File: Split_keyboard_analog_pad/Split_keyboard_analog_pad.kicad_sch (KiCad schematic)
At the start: 138 parts, among them J1 Conn_01x05_Pin, J2 Conn_01x05_Pin, J3 Conn_01x08_Pin, J4 Conn_01x08_Pin, J5 Conn_01x02, J6 Conn_01x02, U1 nice_nano, U2 nice_nano

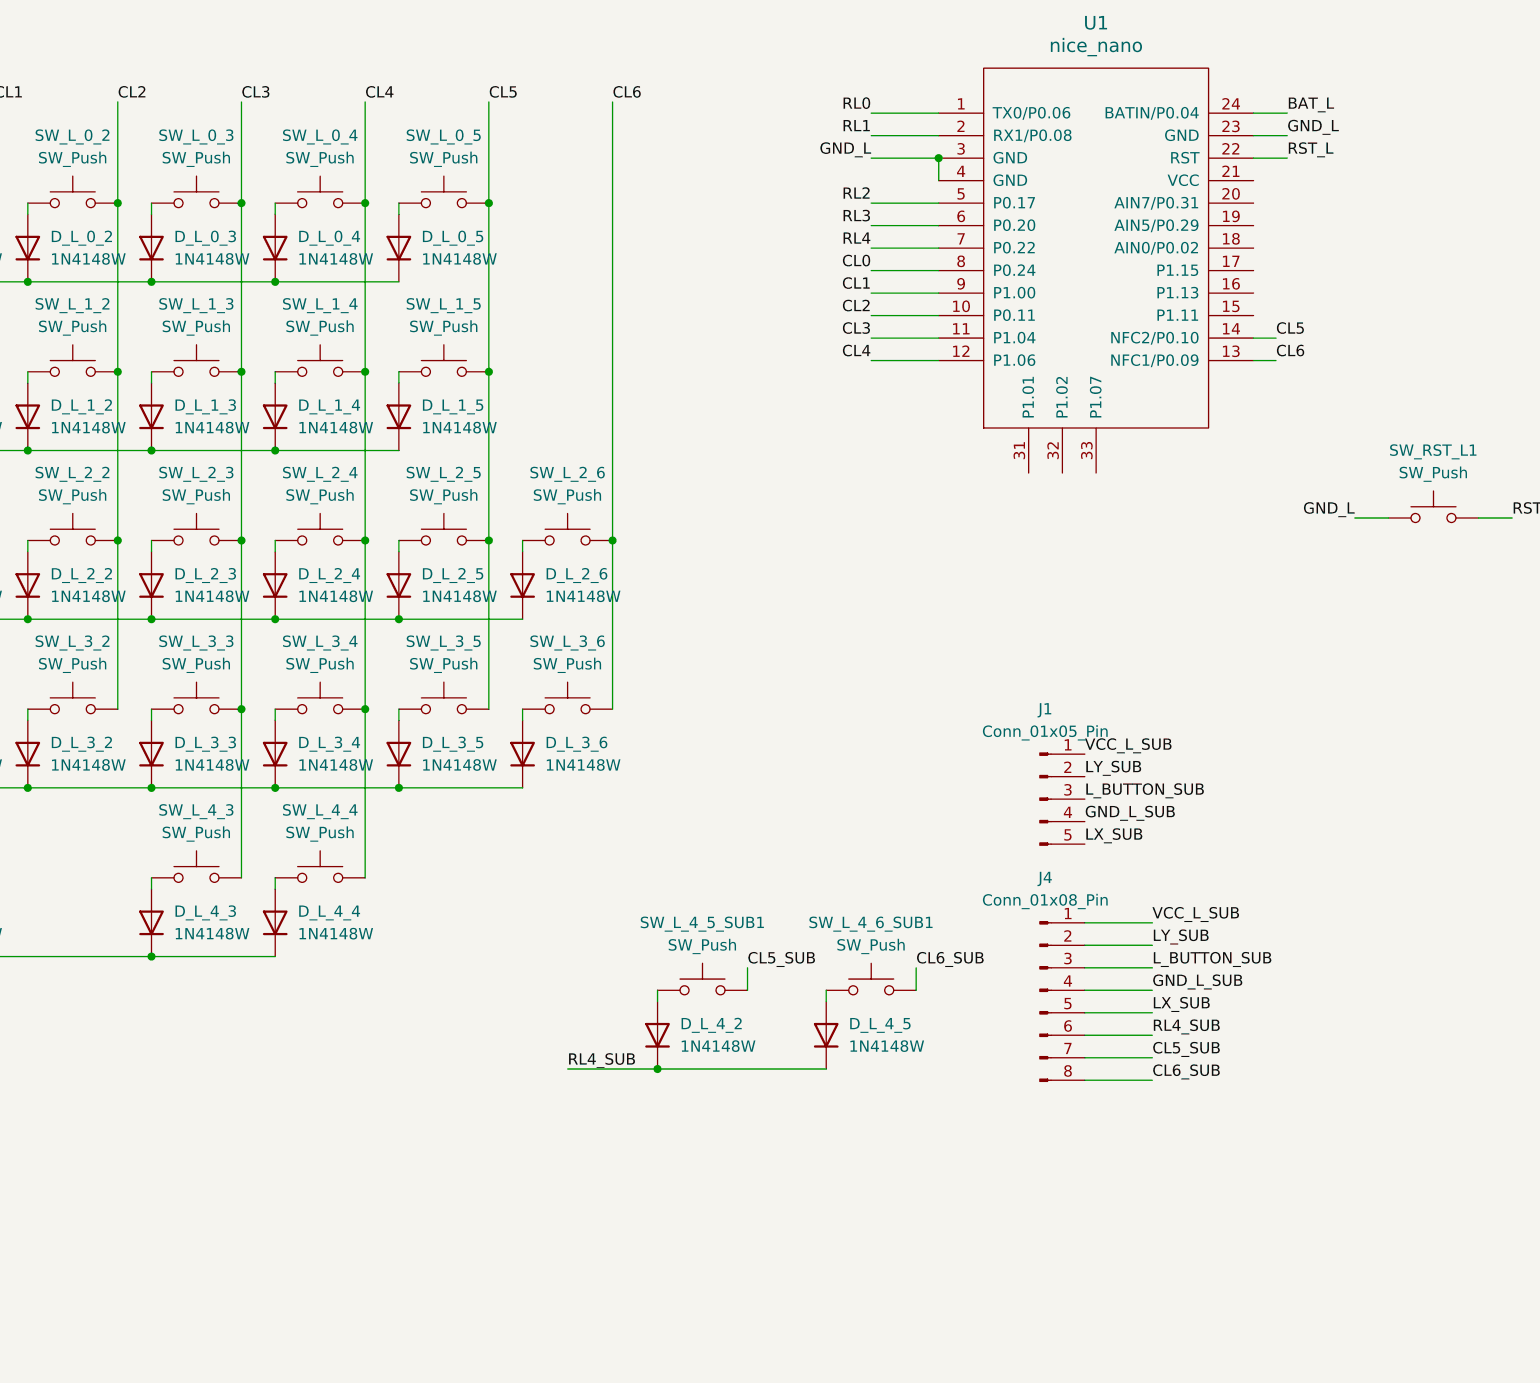
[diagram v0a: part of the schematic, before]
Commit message: remove LED definition
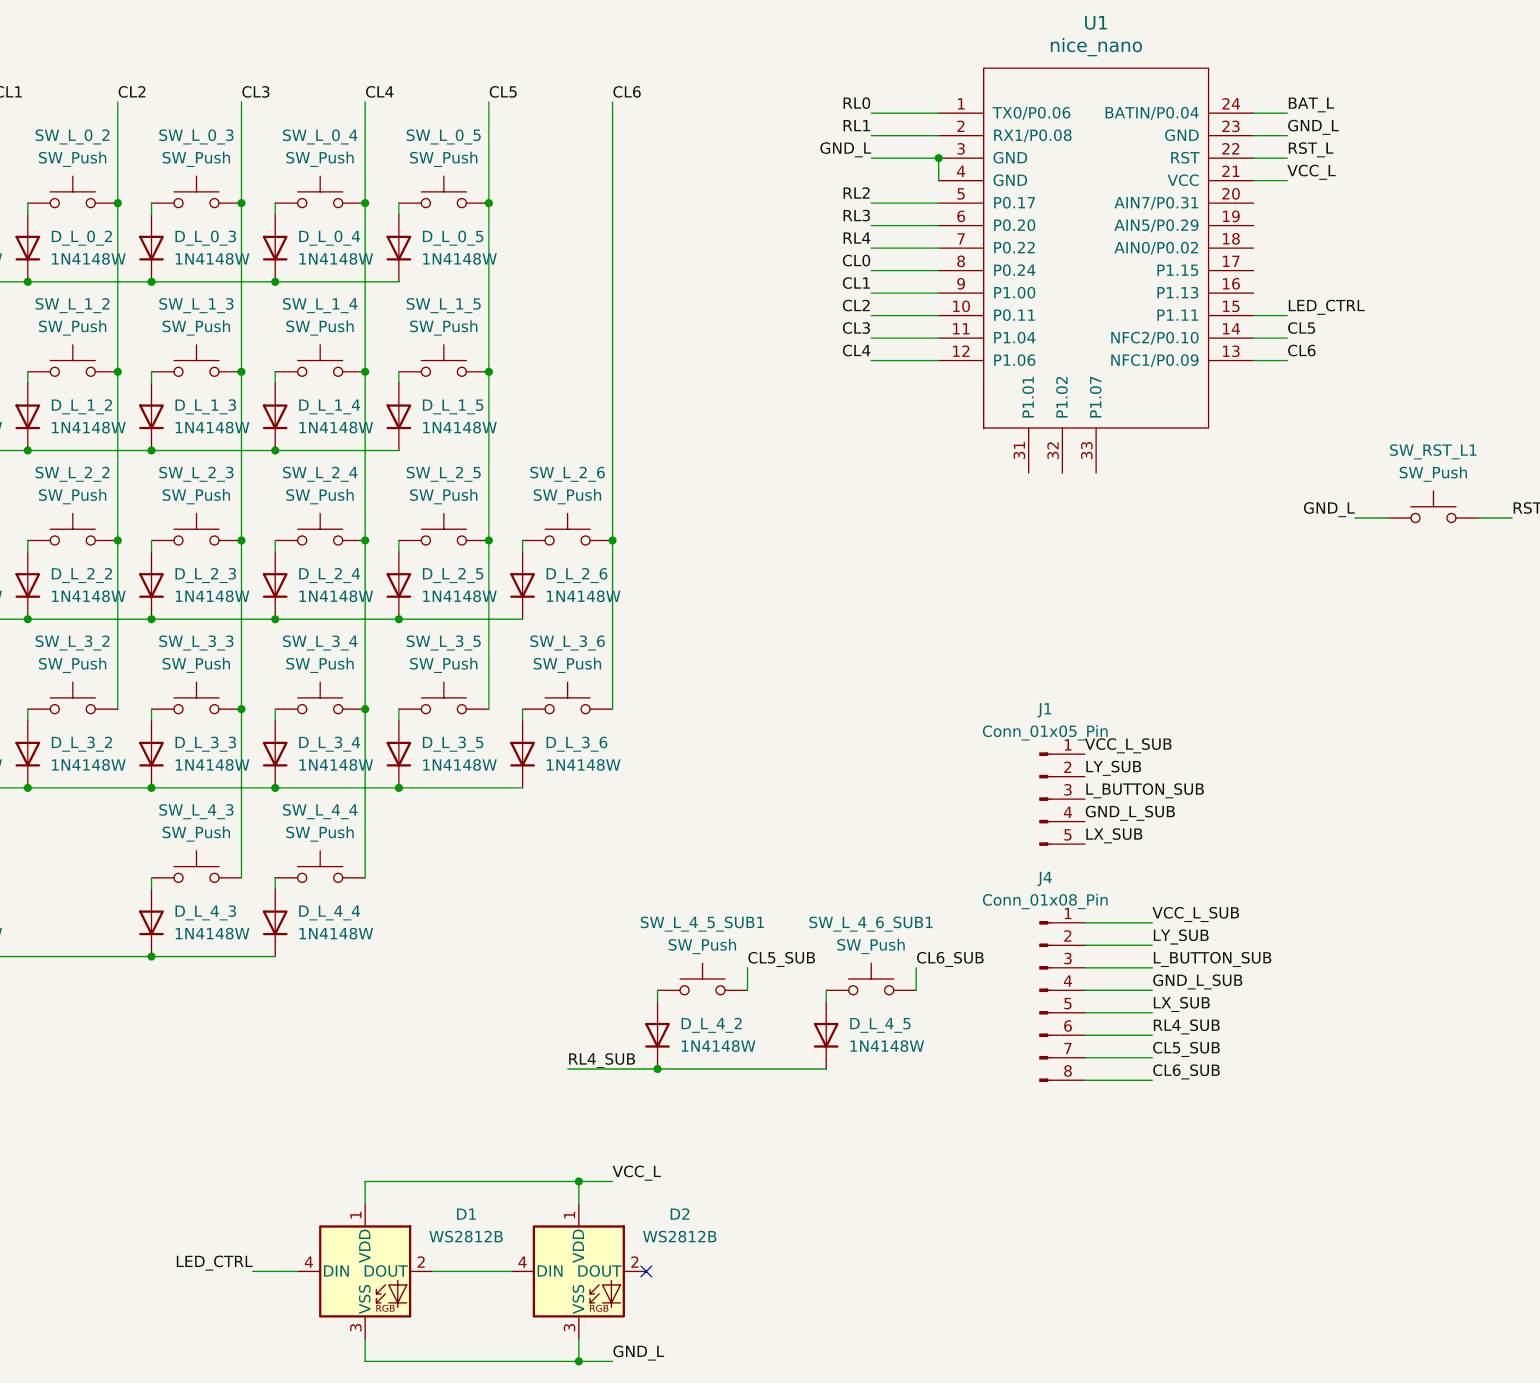
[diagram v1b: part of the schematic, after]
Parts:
- added D1, D2: WS2812B, LED_SMD:LED_WS2812B_PLCC4_5.0x5.0mm_P3.2mm, symbol LED:WS2812B
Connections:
- net GND_L: now also D1.3 (VSS), D2.3 (VSS)
- net LED_CTRL: now reaches U1.15 (P1.11)
- net LED_CTRL: now also D1.4 (DIN)
- net VCC_L: now reaches U1.21 (VCC)
- net VCC_L: now also D1.1 (VDD), D2.1 (VDD)
- new net: D1.2 (DOUT), D2.4 (DIN)
- no-connect marks 0 -> 1
